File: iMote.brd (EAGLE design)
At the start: 43 x 50 mm, 48 parts, among them CN1 USB-MINIB-UX60SC-MB, CN2 ICSP, CN3 CC-HEADER, IC1 ATmega328P-AU, IC2 FT232RLSSOP, IC3 BLE112-A-VISUAL, Q1 16MHz, T1 2SC1815

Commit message: もろもろ余裕を出そうとしている
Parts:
- moved CN2 6.00 mm to (32.4, 4.10)
- moved R2 4.10 mm to (29.6, 12.7), turned to 270 degrees
- moved LED2 2.41 mm to (29.3, 7.70)
- moved R3 2.34 mm to (25.5, 7.70)
- moved RC 2.30 mm to (8.56, 24.3)
- moved R9 2.00 mm to (22.2, 5.50)
- moved S1 1.86 mm to (36.2, 12.1)
- moved C13 1.56 mm to (19.0, 3.39)
- moved Q1 1.40 mm to (7.85, 10.1)
- moved PL-IRM1 1.32 mm to (13.7, 4.20)
- moved LED3 1.10 mm to (15.9, 23.6)
- moved R4 1.00 mm to (37.2, 42.9)
- moved LED1 1.00 mm to (2.60, 42.0)
- moved RB 0.92 mm to (7.39, 17.6)
- moved R5 0.90 mm to (15.9, 27.3)
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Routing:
- net GND: track 117.8 -> 86.4 mm, vias 18 -> 22
- net +5V: track 85.9 -> 98.8 mm
- net D13/SCK: track 9.31 -> 18.5 mm
- net D11/MOSI: track 7.75 -> 15.8 mm, vias 1 -> 2
- net D12/MISO: track 6.31 -> 13.2 mm, vias 1 -> 2
- net +3V3: track 54.2 -> 60.1 mm
- net N$16: track 2.87 -> 5.71 mm
- net N$12: track 2.31 -> 4.13 mm
- net N$8: track 17.8 -> 19.5 mm
- net D8/IRIN: track 8.85 -> 10.1 mm
- net N$11: track 4.16 -> 5.36 mm
- net !RESET: track 38.9 -> 40.1 mm
- net N$2: track 12.1 -> 11.1 mm
- net N$1: track 10.5 -> 11.4 mm
- net D3/IROUT: track 7.41 -> 6.52 mm
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
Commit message: CN4つくった
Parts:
- added CN4: (no value), pinhead:1X02
- moved D1 3.76 mm to (8.31, 26.4)
- moved RC 2.51 mm to (8.36, 21.8)
- moved T1 1.17 mm to (3.40, 20.2)
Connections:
- removed net N$12: D1.C, RC.2
- new net IRLED: CN4.2, D1.C, RC.2
- net +5V: now also CN4.1
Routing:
- net IRLED: track 0.00 -> 9.63 mm
- net +5V: track 98.8 -> 107.3 mm
- net N$12: track 4.13 -> 0.00 mm
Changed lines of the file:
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@@
 </element>
 <element name="C11" library="my" package="E2-5" value="10uF" x="4.348" y="35.212" smashed="yes" rot="R180">
-<attribute name="NAME" x="0.904" y="36.408" size="0.8128" layer="25" rot="R270"/>
+<attribute name="NAME" x="0.804" y="36.408" size="0.8128" layer="25" rot="R270"/>
 <attribute name="VALUE" x="1.808" y="37.371" size="1.27" layer="27" ratio="10" rot="R180"/>
 </element>
@@
 <attribute name="VALUE" x="28.538" y="5.414" size="1.27" layer="27"/>
 </element>
-<element name="T1" library="transistor" package="TO92-ECB" value="2SC1815" x="4.034" y="21.18" smashed="yes" rot="R270">
-<attribute name="NAME" x="0.88" y="20.782" size="0.8128" layer="25"/>
-<attribute name="VALUE" x="0.732" y="23.72" size="1.27" layer="27" ratio="10" rot="R270"/>
+<element name="T1" library="transistor" package="TO92-ECB" value="2SC1815" x="3.4" y="20.2" smashed="yes" rot="R270">
+<attribute name="NAME" x="0.246" y="19.802" size="0.8128" layer="25"/>
+<attribute name="VALUE" x="0.098" y="22.74" size="1.27" layer="27" ratio="10" rot="R270"/>
 </element>
 <element name="RB" library="my" package="2012" value="4.7k" x="7.388" y="17.594" smashed="yes">
@@
 <attribute name="VALUE" x="6.626" y="15.308" size="1.27" layer="27"/>
 </element>
-<element name="RC" library="my" package="2012" value="47" x="8.564" y="24.268" smashed="yes" rot="R90">
-<attribute name="NAME" x="7.748" y="23.706" size="0.8128" layer="25" rot="R90"/>
-<attribute name="VALUE" x="10.85" y="23.506" size="1.27" layer="27" rot="R90"/>
+<element name="RC" library="my" package="2012" value="47" x="8.364" y="21.768" smashed="yes" rot="R90">
+<attribute name="NAME" x="7.548" y="21.206" size="0.8128" layer="25" rot="R90"/>
+<attribute name="VALUE" x="10.65" y="21.006" size="1.27" layer="27" rot="R90"/>
 </element>
 <element name="STANDOFF1" library="SparkFun-Electromechanical" package="STAND-OFF" value="STAND-OFF" x="40" y="3"/>
@@
 <attribute name="VALUE" x="16.758" y="4.15" size="1.27" layer="27" rot="R270"/>
 </element>
-<element name="D1" library="my" package="LED-3MM" value="OSIR5113A" x="5.408" y="28.842" smashed="yes" rot="R270">
-<attribute name="NAME" x="0.948" y="28.718" size="0.8128" layer="21"/>
+<element name="D1" library="my" package="LED-3MM" value="OSIR5113A" x="8.308" y="26.442" smashed="yes" rot="R270">
+<attribute name="NAME" x="5.582" y="23.748" size="0.8128" layer="21" rot="R90"/>
 </element>
 <element name="IC2" library="my" package="SSOP28DB" value="FT232RLSSOP" x="13.336" y="34.744" smashed="yes">
@@
 <attribute name="NAME" x="36.738" y="40.816" size="0.8128" layer="25"/>
 <attribute name="VALUE" x="36.738" y="37.814" size="1.27" layer="27"/>
+</element>
+<element name="CN4" library="pinhead" package="1X02" value="" x="3.6" y="29" smashed="yes" rot="R270">
+<attribute name="NAME" x="1.3288" y="30.2162" size="0.8128" layer="25" rot="R270"/>
+<attribute name="VALUE" x="0.425" y="31.54" size="1.27" layer="27" rot="R270"/>
 </element>
 </elements>
@@
 <wire x1="13.98" y1="13.44" x2="14.0494" y2="13.442" width="0.4572" layer="1"/>
 <wire x1="13.94" y1="11.84" x2="14.0494" y2="11.842" width="0.4572" layer="1"/>
-<wire x1="11.06" y1="31" x2="11.061" y2="31.088" width="0.4572" layer="1"/>
-<wire x1="10.3" y1="14.07" x2="10.3" y2="28.9" width="0.8128" layer="1"/>
 <wire x1="11.06" y1="31.85" x2="14.311" y2="35.111" width="0.4064" layer="1"/>
 <wire x1="11.06" y1="31.25" x2="11.06" y2="31.85" width="0.4064" layer="1"/>
@@
 <wire x1="14.6" y1="41.8" x2="14.6" y2="41.12" width="1.27" layer="1"/>
 <wire x1="14.6" y1="41.12" x2="13.89" y2="40.41" width="1.27" layer="1"/>
-<wire x1="10.3" y1="29.4" x2="10.4" y2="29.3" width="0.8128" layer="1"/>
-<wire x1="10.4" y1="29.3" x2="10.3" y2="28.9" width="0.8128" layer="1"/>
 <wire x1="5.1" y1="41.05" x2="5.264" y2="40.786" width="0.8128" layer="1"/>
 <wire x1="5.264" y1="40.786" x2="5.264" y2="38.696" width="0.8128" layer="1"/>
 <wire x1="5.1" y1="41.05" x2="5.64" y2="40.41" width="0.8128" layer="1"/>
 <wire x1="5.64" y1="40.41" x2="13.89" y2="40.41" width="0.8128" layer="1"/>
-<wire x1="5.408" y1="30.112" x2="5.364" y2="30.156" width="0.8128" layer="1"/>
-<wire x1="5.364" y1="30.156" x2="5.364" y2="35.212" width="0.8128" layer="1"/>
-<wire x1="10.69" y1="29.4" x2="10.3" y2="29.4" width="0.8128" layer="1"/>
-<wire x1="10.3" y1="29.4" x2="9.9" y2="29.4" width="0.8128" layer="1"/>
-<wire x1="11.06" y1="31" x2="11.07" y2="30.99" width="0.5" layer="1" curve="-90"/>
-<wire x1="9.93" y1="29.4" x2="9.9" y2="29.4" width="0.5" layer="1"/>
-<wire x1="11.07" y1="30.99" x2="11.07" y2="29.17" width="0.5" layer="1"/>
-<wire x1="11.07" y1="29.17" x2="10.3" y2="28.9" width="0.5" layer="1" curve="-90"/>
-<wire x1="5.408" y1="30.112" x2="5.42" y2="30.1" width="1.016" layer="1"/>
-<wire x1="5.42" y1="30.1" x2="7.4" y2="30.1" width="1.016" layer="1"/>
-<wire x1="7.4" y1="30.1" x2="8.2" y2="29.3" width="1.016" layer="1"/>
-<wire x1="8.2" y1="29.3" x2="10.4" y2="29.3" width="1.016" layer="1"/>
 <wire x1="11.7" y1="13.45" x2="11.752" y2="13.43" width="0.6096" layer="1"/>
 <wire x1="11.752" y1="13.43" x2="10.94" y2="13.43" width="0.8128" layer="1"/>
@@
 <wire x1="29.9" y1="5.5" x2="29.896" y2="5.504" width="0.5" layer="1"/>
 <wire x1="29.896" y1="5.504" x2="23.132" y2="5.504" width="0.5" layer="1"/>
+<contactref element="CN4" pad="1"/>
+<wire x1="14.2" y1="39.9" x2="14.31" y2="39.62" width="0.4064" layer="1"/>
+<wire x1="14.2" y1="39.9" x2="13.89" y2="40.41" width="0.4064" layer="1"/>
+<wire x1="10.3" y1="14.07" x2="10.3" y2="27.7" width="1.016" layer="1"/>
+<wire x1="10.3" y1="27.7" x2="11.061" y2="28.461" width="0.4064" layer="1"/>
+<wire x1="11.061" y1="28.461" x2="11.061" y2="31.088" width="0.4064" layer="1"/>
+<wire x1="10.3" y1="27.7" x2="8.3" y2="27.7" width="1.27" layer="1"/>
+<wire x1="8.3" y1="27.7" x2="8.1" y2="27.7" width="1.27" layer="1"/>
+<wire x1="8.3" y1="27.7" x2="8.308" y2="27.712" width="0.4064" layer="1"/>
+<wire x1="8.1" y1="27.7" x2="5.4" y2="30.4" width="1.27" layer="1"/>
+<wire x1="5.4" y1="30.4" x2="5.4" y2="35.1" width="1.27" layer="1"/>
+<wire x1="6.12" y1="29.9" x2="8.308" y2="27.712" width="1.27" layer="1"/>
+<wire x1="3.6" y1="30.27" x2="5.75" y2="30.27" width="1.27" layer="1"/>
+<wire x1="5.75" y1="30.27" x2="8.308" y2="27.712" width="1.27" layer="1"/>
 </signal>
 <signal name="N$3">
@@
 <contactref element="T1" pad="B"/>
 <wire x1="6.4" y1="17.6" x2="6.438" y2="17.594" width="0.254" layer="1"/>
-<wire x1="4.034" y1="18.64" x2="5.08" y2="17.594" width="1.016" layer="1"/>
+<wire x1="3.4" y1="17.66" x2="5.08" y2="17.594" width="1.016" layer="1"/>
 <wire x1="5.08" y1="17.594" x2="6.438" y2="17.594" width="1.016" layer="1"/>
 </signal>
@@
 <contactref element="RC" pad="1"/>
 <contactref element="T1" pad="C"/>
-<wire x1="8.564" y1="23.318" x2="6.226" y2="21.18" width="1.016" layer="1"/>
-<wire x1="6.226" y1="21.18" x2="4.034" y2="21.18" width="1.016" layer="1"/>
-</signal>
-<signal name="N$12" class="2">
+<wire x1="8.364" y1="20.818" x2="4.018" y2="20.818" width="1.016" layer="1"/>
+<wire x1="4.018" y1="20.818" x2="3.4" y2="20.2" width="1.016" layer="1"/>
+</signal>
+<signal name="IRLED" class="2">
+<contactref element="CN4" pad="2"/>
 <contactref element="RC" pad="2"/>
 <contactref element="D1" pad="C"/>
-<wire x1="5.408" y1="27.572" x2="6.21" y2="27.572" width="1.016" layer="1"/>
-<wire x1="6.21" y1="27.572" x2="8.564" y2="25.218" width="1.016" layer="1"/>
+<wire x1="3.6" y1="25.3" x2="7.8" y2="25.3" width="1.016" layer="1"/>
+<wire x1="3.6" y1="27.4" x2="3.6" y2="25.3" width="1.016" layer="1"/>
+<wire x1="7.8" y1="25.3" x2="8.308" y2="25.172" width="1.016" layer="1"/>
+<wire x1="3.6" y1="27.4" x2="3.6" y2="27.73" width="1.016" layer="1"/>
+<wire x1="8.364" y1="22.718" x2="8.364" y2="25.116" width="1.016" layer="1"/>
+<wire x1="8.364" y1="25.116" x2="8.308" y2="25.172" width="1.016" layer="1"/>
 </signal>
 <signal name="+3V3" class="4">
@@
 <contactref element="RB" pad="2"/>
 <wire x1="14" y1="15.9" x2="14.0494" y2="15.842" width="0.254" layer="1"/>
-<via x="9.3" y="17.6" extent="1-16" drill="0.3"/>
-<via x="11.3" y="17.6" extent="1-16" drill="0.3"/>
-<wire x1="9.3" y1="17.6" x2="11.3" y2="17.6" width="0.4064" layer="16"/>
-<wire x1="9.3" y1="17.6" x2="8.4" y2="17.6" width="0.6096" layer="1"/>
+<via x="9.2" y="17.6" extent="1-16" drill="0.3"/>
+<via x="11.4" y="17.6" extent="1-16" drill="0.3"/>
+<wire x1="9.2" y1="17.6" x2="11.4" y2="17.6" width="0.4064" layer="16"/>
+<wire x1="9.2" y1="17.6" x2="8.4" y2="17.6" width="0.6096" layer="1"/>
 <wire x1="8.4" y1="17.6" x2="8.338" y2="17.594" width="0.254" layer="1"/>
-<wire x1="11.3" y1="17.6" x2="12.2914" y2="17.6" width="0.6096" layer="1"/>
+<wire x1="11.4" y1="17.6" x2="12.2914" y2="17.6" width="0.6096" layer="1"/>
 <wire x1="12.2914" y1="17.6" x2="14.0494" y2="15.842" width="0.6096" layer="1"/>
 </signal>

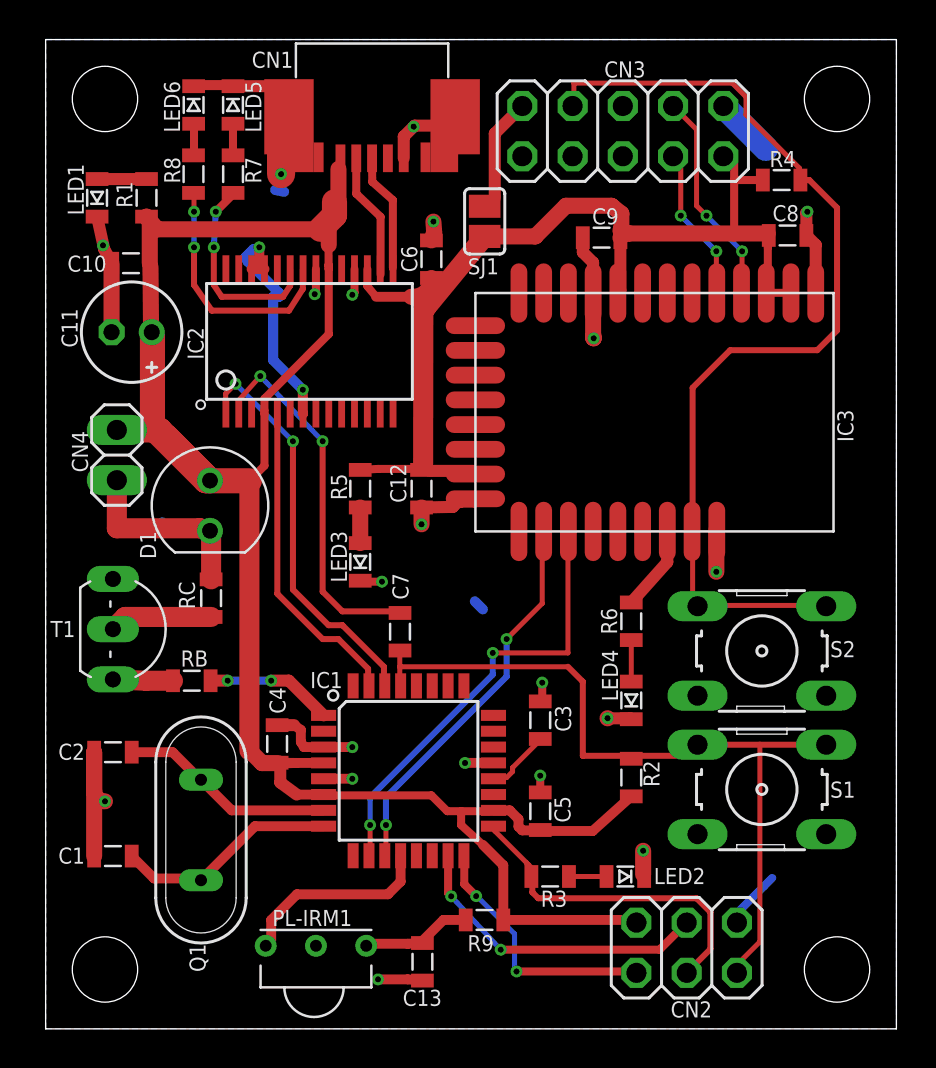
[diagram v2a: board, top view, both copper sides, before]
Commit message: IC3をちょっと右へ動かした
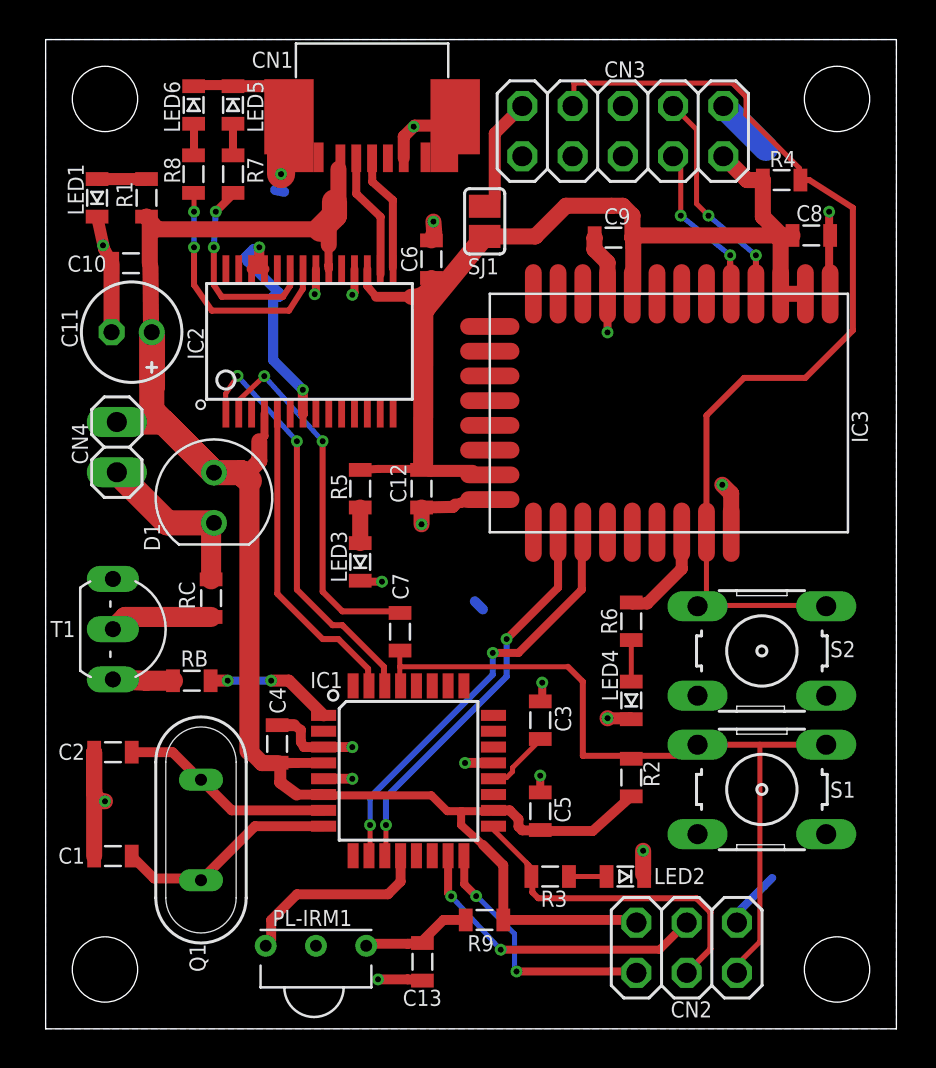
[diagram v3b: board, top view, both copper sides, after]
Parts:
- moved C8 1.20 mm to (38.7, 40.1)
- moved IC3 0.73 mm to (31.5, 31.1)
- moved C9 0.60 mm to (28.7, 40.0)
- moved D1 0.45 mm to (8.51, 26.8)
- moved CN4 0.40 mm to (3.60, 29.4)
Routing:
- net +5V: track 107.3 -> 98.0 mm
- net +3V3: track 60.1 -> 61.9 mm
- net D6/BLERX: track 22.8 -> 21.6 mm
- net BLE/P0_0: track 4.28 -> 5.20 mm
- net IRLED: track 9.63 -> 8.84 mm
- net GND: track 86.4 -> 85.8 mm
- net D0/USBRX: track 20.5 -> 21.1 mm

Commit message: 3.3v周り微調整
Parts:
- moved C10 0.50 mm to (4.81, 38.7)
- moved C11 0.20 mm to (4.55, 35.2)
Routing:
- net +5V: track 98.0 -> 91.9 mm
- net +3V3: track 61.9 -> 60.4 mm
- net GND: track 85.8 -> 86.5 mm
